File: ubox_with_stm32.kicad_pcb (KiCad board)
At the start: 2 copper layers, 45.6 x 23 mm, 21 parts, among them J1 I2c_pin, J3 UART_Pin, U3 SAM-M10Q-00B

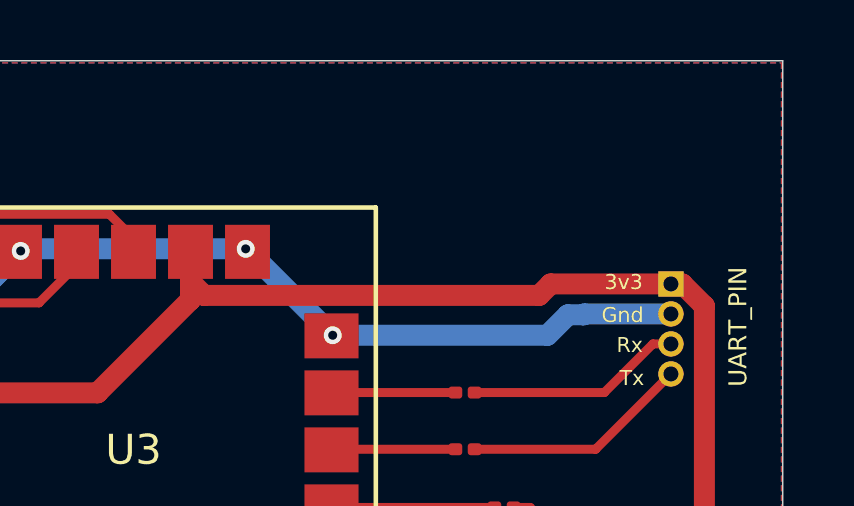
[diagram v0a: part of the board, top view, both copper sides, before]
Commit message: add decoupling
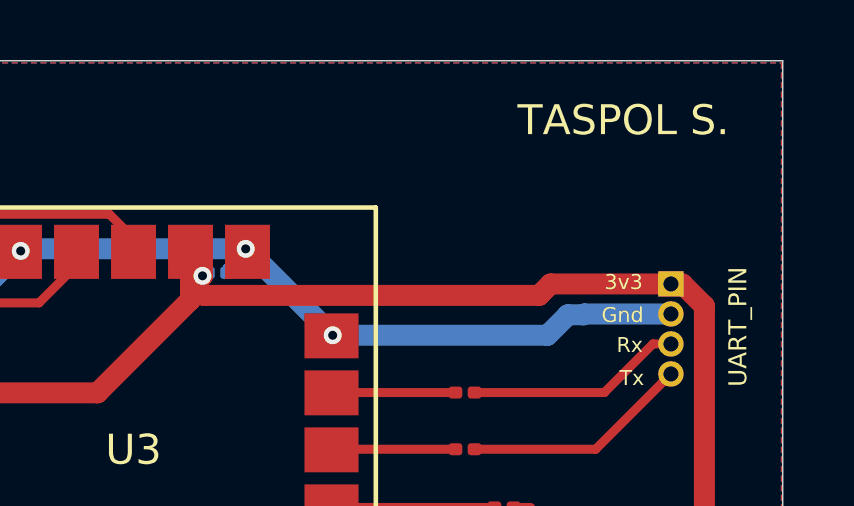
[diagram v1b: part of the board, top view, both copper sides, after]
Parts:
- added C2: 1.0 µF, Capacitor_SMD:C_0201_0603Metric, B.Cu at (153.8, 63.6)
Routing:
- net GND: track 91.7 -> 92.8 mm
- net 3.3V: track 71.7 -> 72.0 mm, vias 4 -> 5
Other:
- board text added: "TASPOL S."

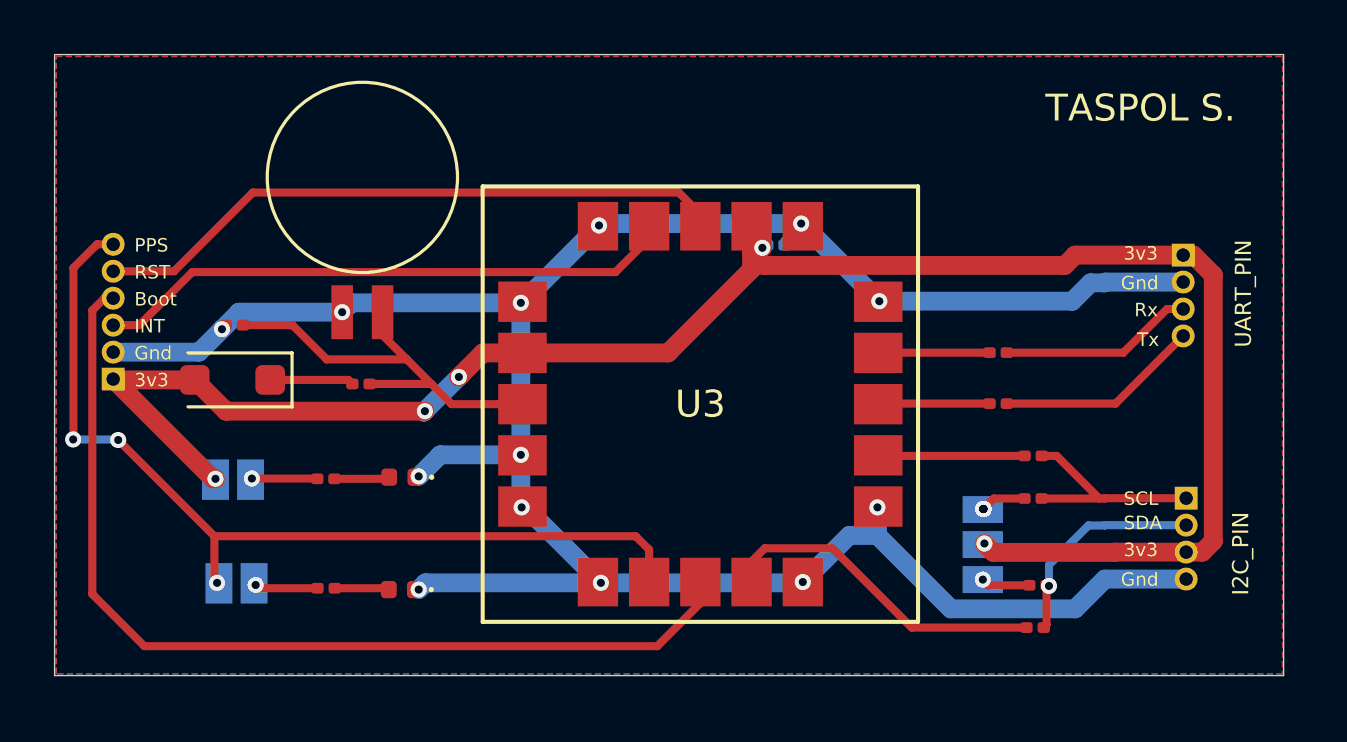
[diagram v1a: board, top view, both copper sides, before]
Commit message: resize component
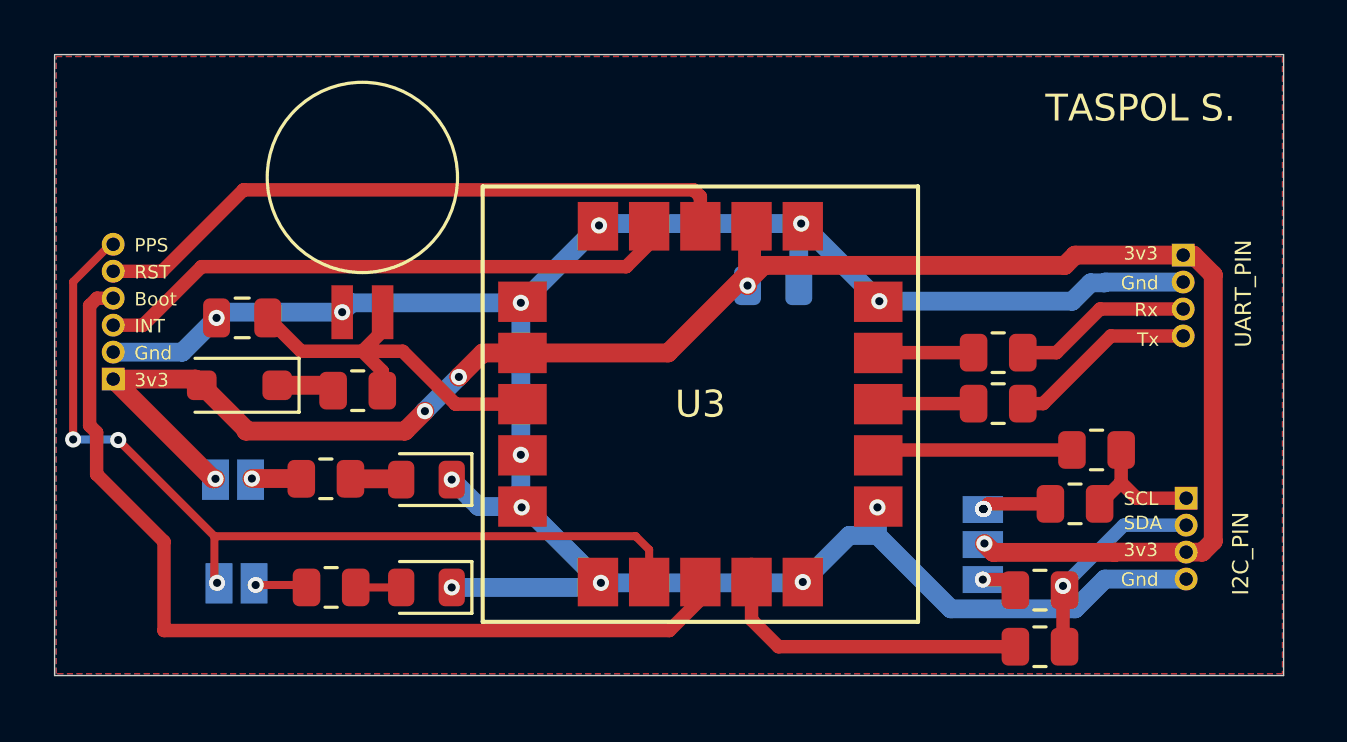
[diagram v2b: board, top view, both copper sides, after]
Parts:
- C1, C2: footprint Capacitor_SMD:C_0201_0603Metric -> Capacitor_SMD:C_0805_2012Metric
- D2, D3: footprint LED_SMD:LED_0402_1005Metric -> LED_SMD:LED_0805_2012Metric
- R1, R2, R3, R4, R5, R6, R7, R8, R9: footprint Resistor_SMD:R_0201_0603Metric -> Resistor_SMD:R_0805_2012Metric
- moved R4 2.36 mm to (165.7, 71.2)
- moved R7 1.57 mm to (164.9, 73.2)
- moved C2 1.50 mm to (153.7, 65.1)
- moved D2 0.92 mm to (140.8, 76.3)
- moved D3 0.90 mm to (140.8, 72.3)
- moved R5 0.73 mm to (163.6, 78.5)
- moved C1 0.40 mm to (134.0, 66.3)
- moved D1 0.33 mm to (133.9, 68.8)
- moved R1 0.28 mm to (138.3, 69.0)
- moved R6 0.20 mm to (163.6, 76.4)
- moved R2 0.19 mm to (137.3, 76.3)
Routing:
- net SCL: track 8.15 -> 5.00 mm
- net T1: track 5.44 -> 7.44 mm
- net 3.3V: track 72.0 -> 73.8 mm
- net Backup: track 16.0 -> 14.3 mm
- net GND: track 92.8 -> 91.6 mm
- net Net-(D1-K): track 3.11 -> 2.16 mm
- net Reset: track 23.8 -> 24.7 mm
- net Net-(JP3-A): track 1.69 -> 2.57 mm
- net TX: track 7.58 -> 6.99 mm
- net RX: track 7.22 -> 6.62 mm
- net Net-(U3-TXD): track 4.14 -> 3.55 mm
- net Net-(U3-RXD): track 4.13 -> 3.54 mm
- net Net-(JP2-A): track 2.43 -> 1.84 mm
- net INT: track 21.7 -> 22.2 mm

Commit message: compatible with breadboard
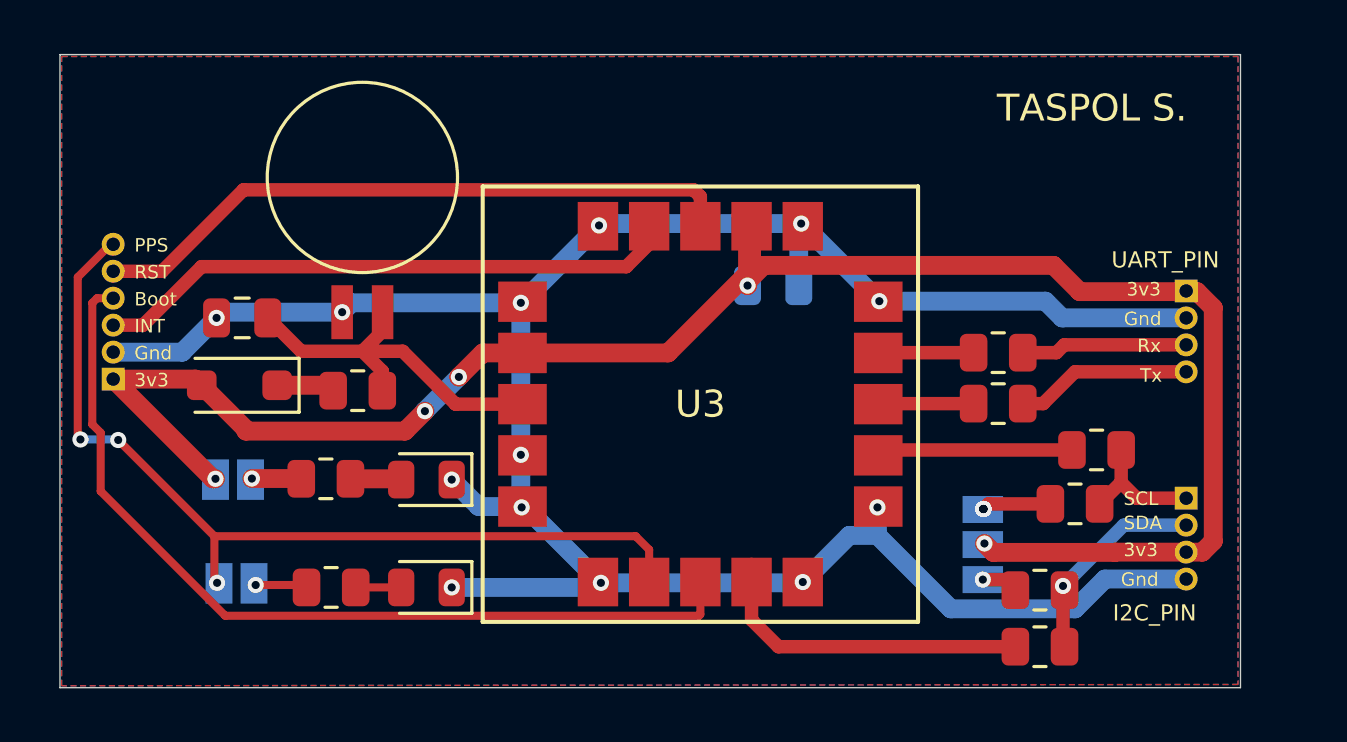
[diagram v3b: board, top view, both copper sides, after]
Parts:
- J1, J3: footprint Connector_PinHeader_1.00mm:PinHeader_1x04_P1.00mm_Horizontal -> Connector_PinHeader_1.00mm:PinHeader_1x04_P1.00mm_Vertical; moved to B.Cu
- J2: footprint Connector_PinHeader_1.00mm:PinHeader_1x06_P1.00mm_Horizontal -> Connector_PinHeader_1.00mm:PinHeader_1x06_P1.00mm_Vertical; moved to B.Cu
- moved J3 1.33 mm to (169.0, 65.3), turned to 180 degrees
- turned J1 to 180 degrees
- turned J2 to 0 degrees
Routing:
- net SafeBoot: track 36.0 -> 34.0 mm
- net 3.3V: track 73.8 -> 72.8 mm
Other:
- board size 45.6 x 23 mm -> 43.8 x 23.5 mm

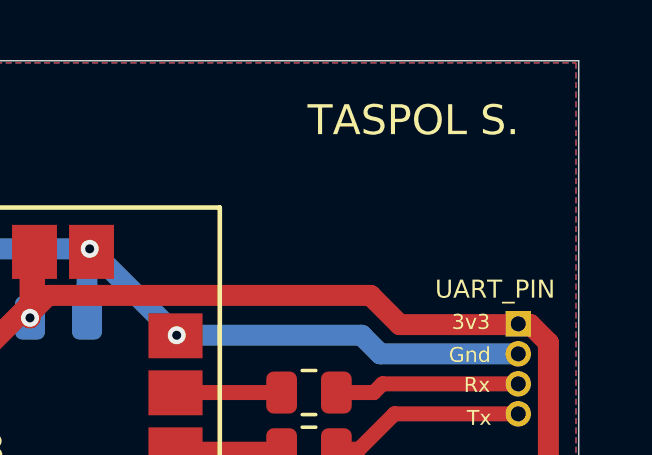
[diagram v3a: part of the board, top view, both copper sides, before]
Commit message: feat: add fabrication & silkscreen
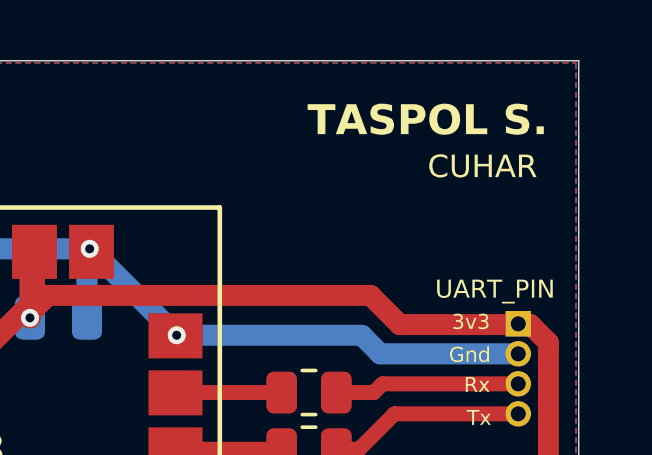
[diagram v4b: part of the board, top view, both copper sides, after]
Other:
- board text added: "CUHAR"
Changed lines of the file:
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@@
 		(tags "Through hole pin header THT 1x06 1.00mm single row")
 		(property "Reference" "J2"
-			(at 0 1.56 360)
+			(at 0 1.56 0)
 			(layer "B.SilkS")
 			(hide yes)
@@
 		)
 		(property "Value" "~"
-			(at 0 -6.56 360)
+			(at 0 -6.56 0)
 			(layer "B.Fab")
 			(hide yes)
@@
 		)
 	)
+	(gr_text "CUHAR"
+		(at 166 60.5 0)
+		(layer "F.SilkS")
+		(effects
+			(font
+				(size 0.75 0.75)
+				(thickness 0.15)
+			)
+			(justify left bottom)
+		)
+	)
 	(gr_text "3v3"
 		(at 166.81 65.53 0)
@@
 			(font
 				(size 1 1)
-				(thickness 0.1)
-			)
-			(justify left bottom)
+				(thickness 0.2)
+				(bold yes)
+			)
+			(justify left bottom)
